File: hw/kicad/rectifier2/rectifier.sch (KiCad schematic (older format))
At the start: 10 parts, among them P1 CONN_01X03, P2 CONN_01X02, P3 CONN_01X02

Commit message: rectifier 2
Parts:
- C1, C2: footprint stmbl:C_Radial_D26_L45_P10 -> Capacitors_ThroughHole:CP_Radial_D35.0mm_P10.00mm_SnapIn
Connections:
- net Earth_Protective: now also P1.3 (P3); no longer P1.1 (P1)
- net at C1.1, C2.1, D1.3 (+): now also P3.2 (P2); no longer P3.1 (P1)
- net at C1.2, C2.2, D1.1 (-): now also P3.1 (P1); no longer P3.2 (P2)
- net at F1.2: now also P1.1 (P1); no longer P1.3 (P3)
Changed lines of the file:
@@
 LIBS:contrib
 LIBS:valves
-LIBS:stmbl
 LIBS:relays
 LIBS:rectifier-cache
-EELAYER 26 0
+EELAYER 25 0
 EELAYER END
 $Descr A4 11693 8268
@@
 F 3 "" H 6200 2150 50  0001 C CNN
 	1    8750 2700
-	1    0    0    -1
+	1    0    0    1
 $EndComp
 $Comp
@@
 F 3 "" H -1100 -2550 50  0001 C CNN
 	1    1850 2900
-	-1   0    0    1
+	-1   0    0    -1
 $EndComp
 $Comp
@@
 F 0 "C1" H 7868 2746 50  0000 L CNN
 F 1 "CP" H 7868 2655 50  0000 L CNN
-F 2 "stmbl:C_Radial_D26_L45_P10" H 5688 750 50  0001 C CNN
+F 2 "Capacitors_ThroughHole:CP_Radial_D35.0mm_P10.00mm_SnapIn" H 5688 750 50  0001 C CNN
 F 3 "" H 5650 900 50  0001 C CNN
 	1    7750 2700
@@
 F 0 "C2" H 8268 2746 50  0000 L CNN
 F 1 "CP" H 8268 2655 50  0000 L CNN
-F 2 "stmbl:C_Radial_D26_L45_P10" H 5488 850 50  0001 C CNN
+F 2 "Capacitors_ThroughHole:CP_Radial_D35.0mm_P10.00mm_SnapIn" H 5488 850 50  0001 C CNN
 F 3 "" H 5450 1000 50  0001 C CNN
 	1    8150 2700

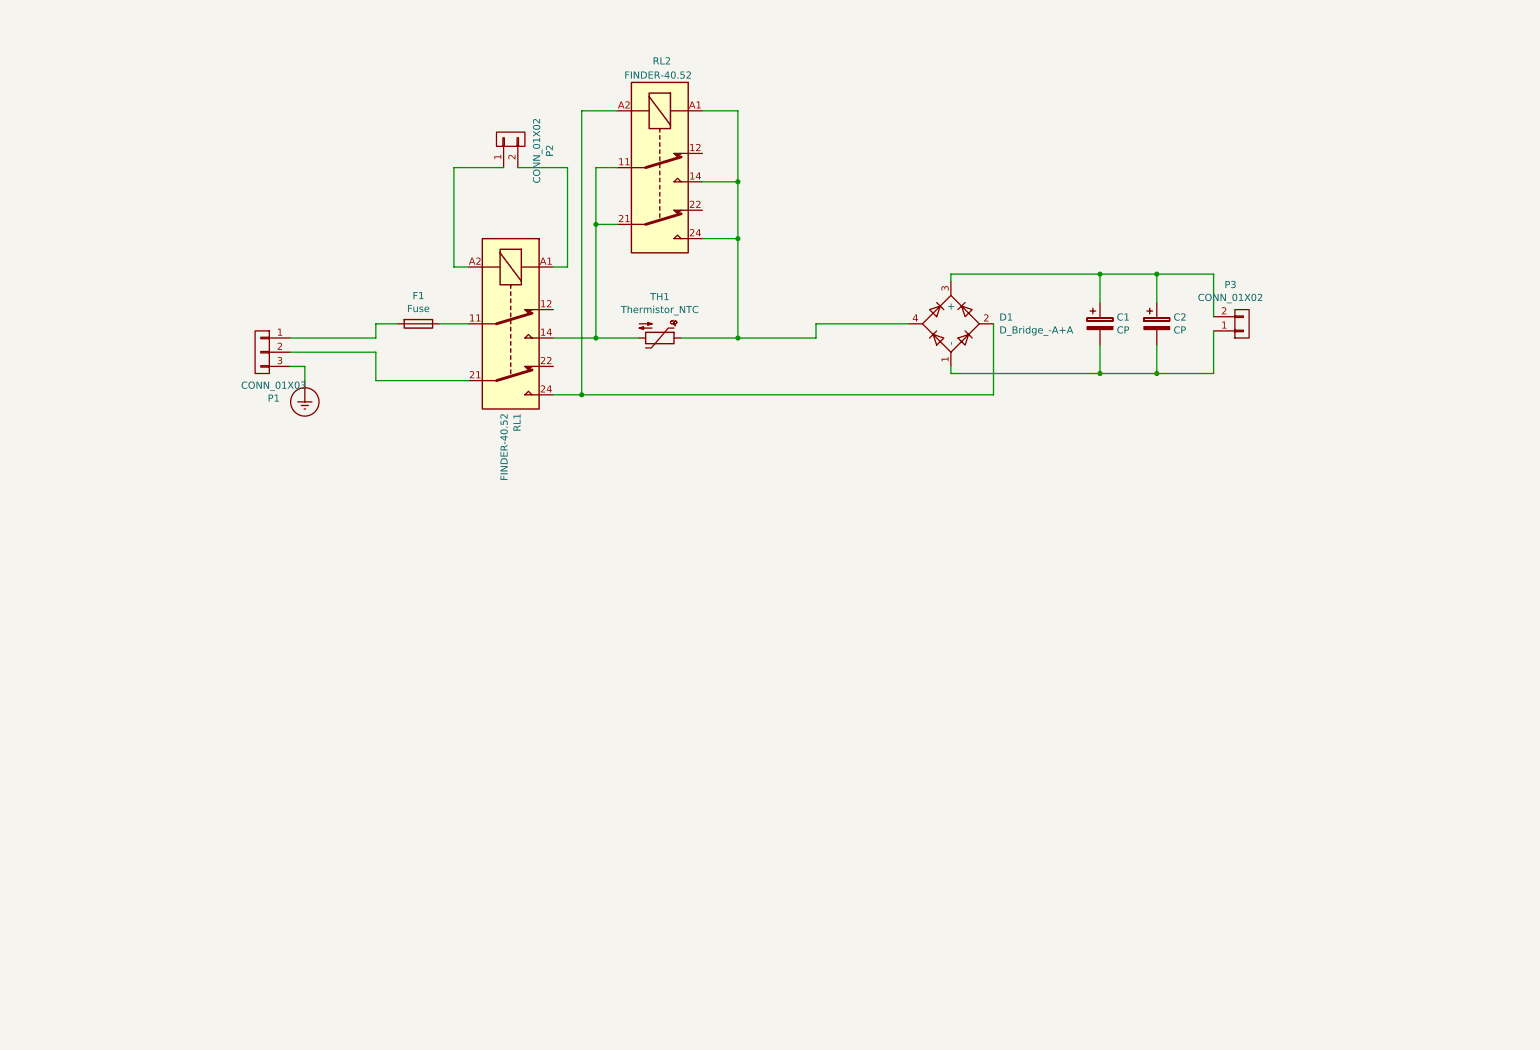
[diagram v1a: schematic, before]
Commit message: Added STM32F042 to rectifier for brake support and proper inrush protection.
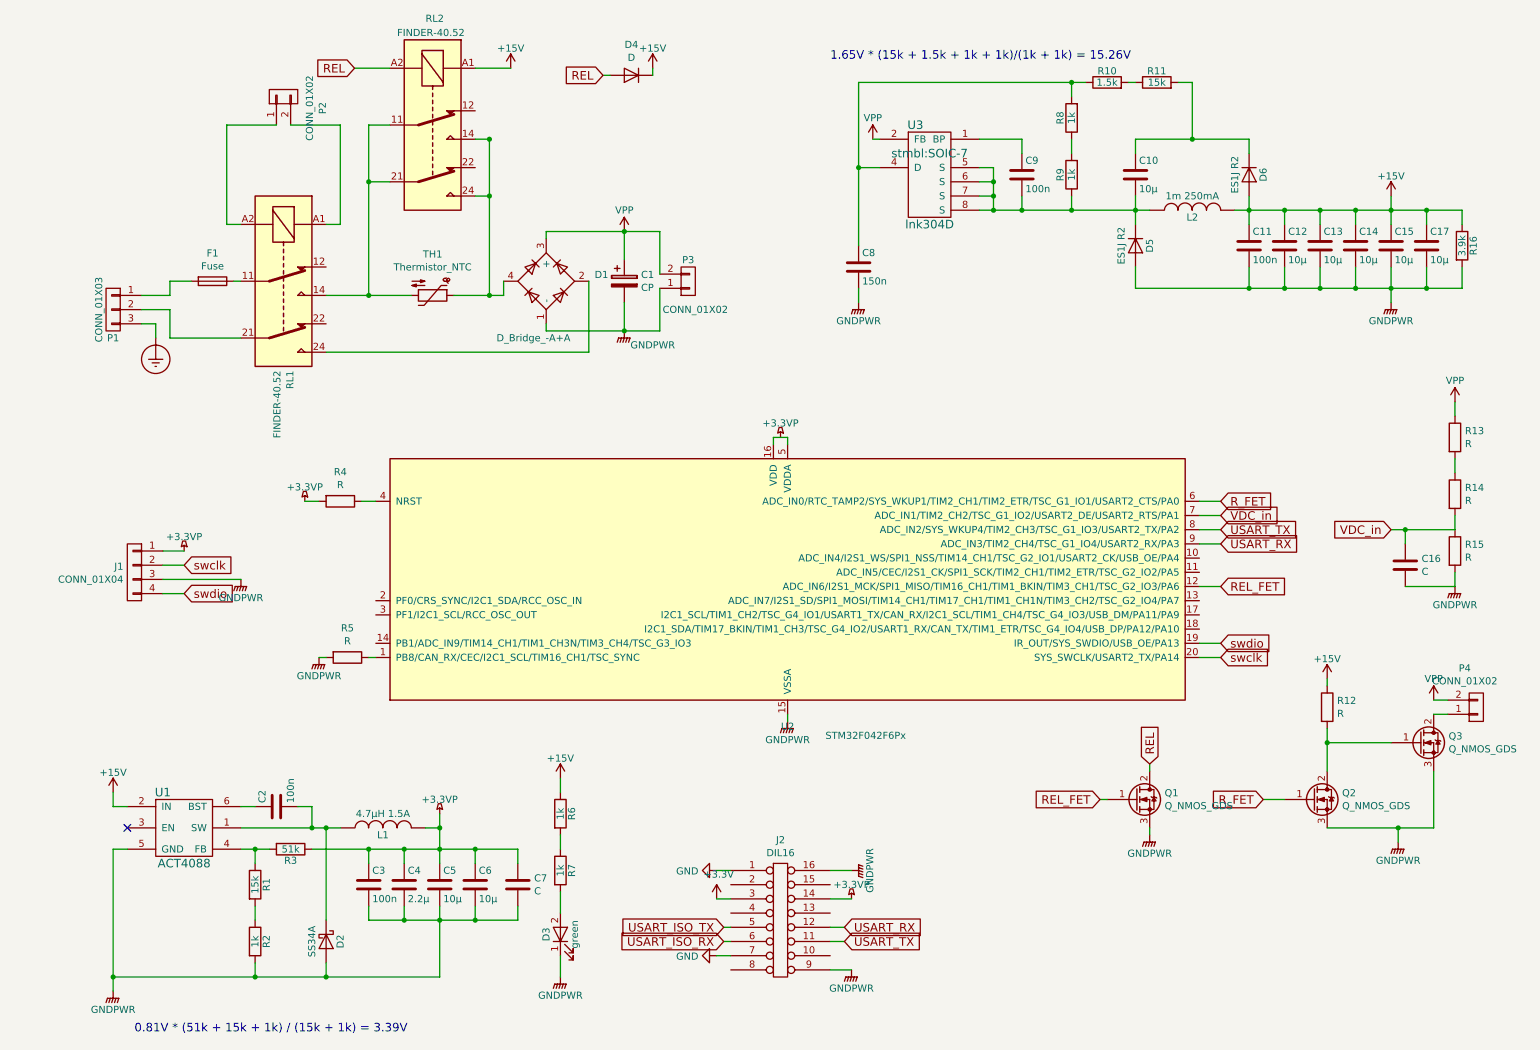
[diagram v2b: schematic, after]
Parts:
- removed C2: CP, Capacitors_ThroughHole:CP_Radial_D35.0mm_P10.00mm_SnapIn, symbol CP
- added C10, C12, C13, C14, C15, C17, C5, C6: 10µ, stmbl:C_0805, symbol C
- added C11, C2, C3, C9: 100n, stmbl:C_0603, symbol C
- added C16, C7: C, symbol C
- added C4: 2.2µ, stmbl:C_0603, symbol C
- added C8: 150n, stmbl:C_1808, symbol C
- added D2: SS34A, stmbl:SMA_Standard, symbol D_Schottky
- added D3: green, stmbl:LED-0805-SIDE, symbol LED
- added D4: D, symbol D
- added D5, D6: ES1J R2, stmbl:SMA_Standard, symbol D
- added J1: CONN_01X04, symbol CONN_01X04
- added J2: DIL16, symbol DIL16
- added L1: 4.7µH 1.5A, stmbl:SMD_INDUCTOR_32x25, symbol INDUCTOR
- added L2: 1m 250mA, stmbl:NPI31W, symbol INDUCTOR
- added P4: CONN_01X02, stmbl:RM5.08_1x2, symbol CONN_01X02
- added Q1, Q2, Q3: Q_NMOS_GDS, symbol Q_NMOS_GDS
- added R1, R11: 15k, stmbl:R_0603, symbol R
- added R10: 1.5k, stmbl:R_0603, symbol R
- added R12, R13, R14, R15, R4, R5: R, symbol R
- added R16: 3.9k, stmbl:R_0603, symbol R
- added R2, R6, R7, R8, R9: 1k, stmbl:R_0603, symbol R
- added R3: 51k, stmbl:R_0603, symbol R
- added U1: ACT4088, TO_SOT_Packages_SMD:SOT-23-6, symbol ACT4088
- added U2: STM32F042F6Px, Housings_SSOP:TSSOP-20_4.4x6.5mm_Pitch0.65mm, symbol STM32F042F6Px
- added U3: lnk304D, stmbl:SOIC-7, symbol lnk304D
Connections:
- net GNDPWR: now reaches C1.2, D1.1 (-), P3.1 (P1)
- net GNDPWR: now also C11.2, C12.2, C13.2, C14.2, C15.2, C16.2, C17.2, C3.2, C4.2, C5.2, C6.2, C7.2, C8.2, D2.2 (A), D3.1 (K), D5.2 (A), J1.3 (P3), J2.16, J2.9, Q1.3 (S), Q2.3 (S), Q3.3 (S), R15.2, R16.2, R2.2, R5.2, U1.5 (GND), U2.15 (VSSA)
- net VPP: now reaches C1.1, D1.3 (+), P3.2 (P2)
- net VPP: now also P4.2 (P2), R13.1, U3.2 (FB)
- net at D1.2, RL1.24: no longer RL2.A2
- net at D1.4, RL2.14, RL2.24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: no longer RL2.A1
- new net: C10.2, C9.2, D5.1 (K), L2.1, R9.1, U3.5 (S), U3.6 (S), U3.7 (S), U3.8 (S)
- new net: C10.1, D6.1 (K), R11.2
- new net: C9.1, U3.1 (BP)
- new net: R8.1, R9.2
- new net: R10.2, R11.1
- new net: D3.2 (A), R7.2
- new net: R6.2, R7.1
- new net: R1.1, R3.2, U1.4 (FB)
- new net: R1.2, R2.1
- new net: C2.2, D2.1 (K), L1.1, U1.1 (SW)
- new net: C2.1, U1.6 (BST)
- new net: C8.1, R10.1, R8.2, U3.4 (D)
- new net: R5.1, U2.1 (PB8/CAN_RX/CEC/I2C1_SCL/TIM16_CH1/TSC_SYNC)
- new net: U2.16 (VDD), U2.5 (VDDA)
- new net: R4.1, U2.4 (NRST)
- new net: R13.2, R14.1
- new net: Q2.2 (D), Q3.1 (G), R12.2
- new net: P4.1 (P1), Q3.2 (D)
- new net +15V: C11.1, C12.1, C13.1, C14.1, C15.1, C17.1, D4.1 (K), D6.2 (A), L2.2, R12.1, R16.1, R6.1, RL2.A1, U1.2 (IN)
- new net +3.3VP: C3.1, C4.1, C5.1, C6.1, C7.1, J1.1 (P1), J2.14, L1.2, R3.1, R4.2
- new net +3V3: J2.3
- new net GND: J2.1, J2.7
- new net REL: D4.2 (A), Q1.2 (D), RL2.A2
- new net REL_FET: Q1.1 (G), U2.12 (ADC_IN6/I2S1_MCK/SPI1_MISO/TIM16_CH1/TIM1_BKIN/TIM3_CH1/TSC_G2_IO3/PA6)
- new net R_FET: Q2.1 (G), U2.6 (ADC_IN0/RTC_TAMP2/SYS_WKUP1/TIM2_CH1/TIM2_ETR/TSC_G1_IO1/USART2_CTS/PA0)
- new net USART_ISO_RX: J2.6
- new net USART_ISO_TX: J2.5
- new net USART_RX: J2.12, U2.9 (ADC_IN3/TIM2_CH4/TSC_G1_IO4/USART2_RX/PA3)
- new net USART_TX: J2.11, U2.8 (ADC_IN2/SYS_WKUP4/TIM2_CH3/TSC_G1_IO3/USART2_TX/PA2)
- new net VDC_in: C16.1, R14.2, R15.1, U2.7 (ADC_IN1/TIM2_CH2/TSC_G1_IO2/USART2_DE/USART2_RTS/PA1)
- new net swclk: J1.2 (P2), U2.20 (SYS_SWCLK/USART2_TX/PA14)
- new net swdio: J1.4 (P4), U2.19 (IR_OUT/SYS_SWDIO/USB_OE/PA13)
- no-connect marks 0 -> 1
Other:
- note added: "0.81V * (51k + 15k + 1k) / (15k + 1k) = 3.39V"
- note added: "1.65V * (15k + 1.5k + 1k + 1k)/(1k + 1k) = 15.26V"
- moved on the sheet: C1, D1, F1, P1, P2, P3, RL1, RL2, TH1

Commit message: Change relay drive to 24V and add enable feedback
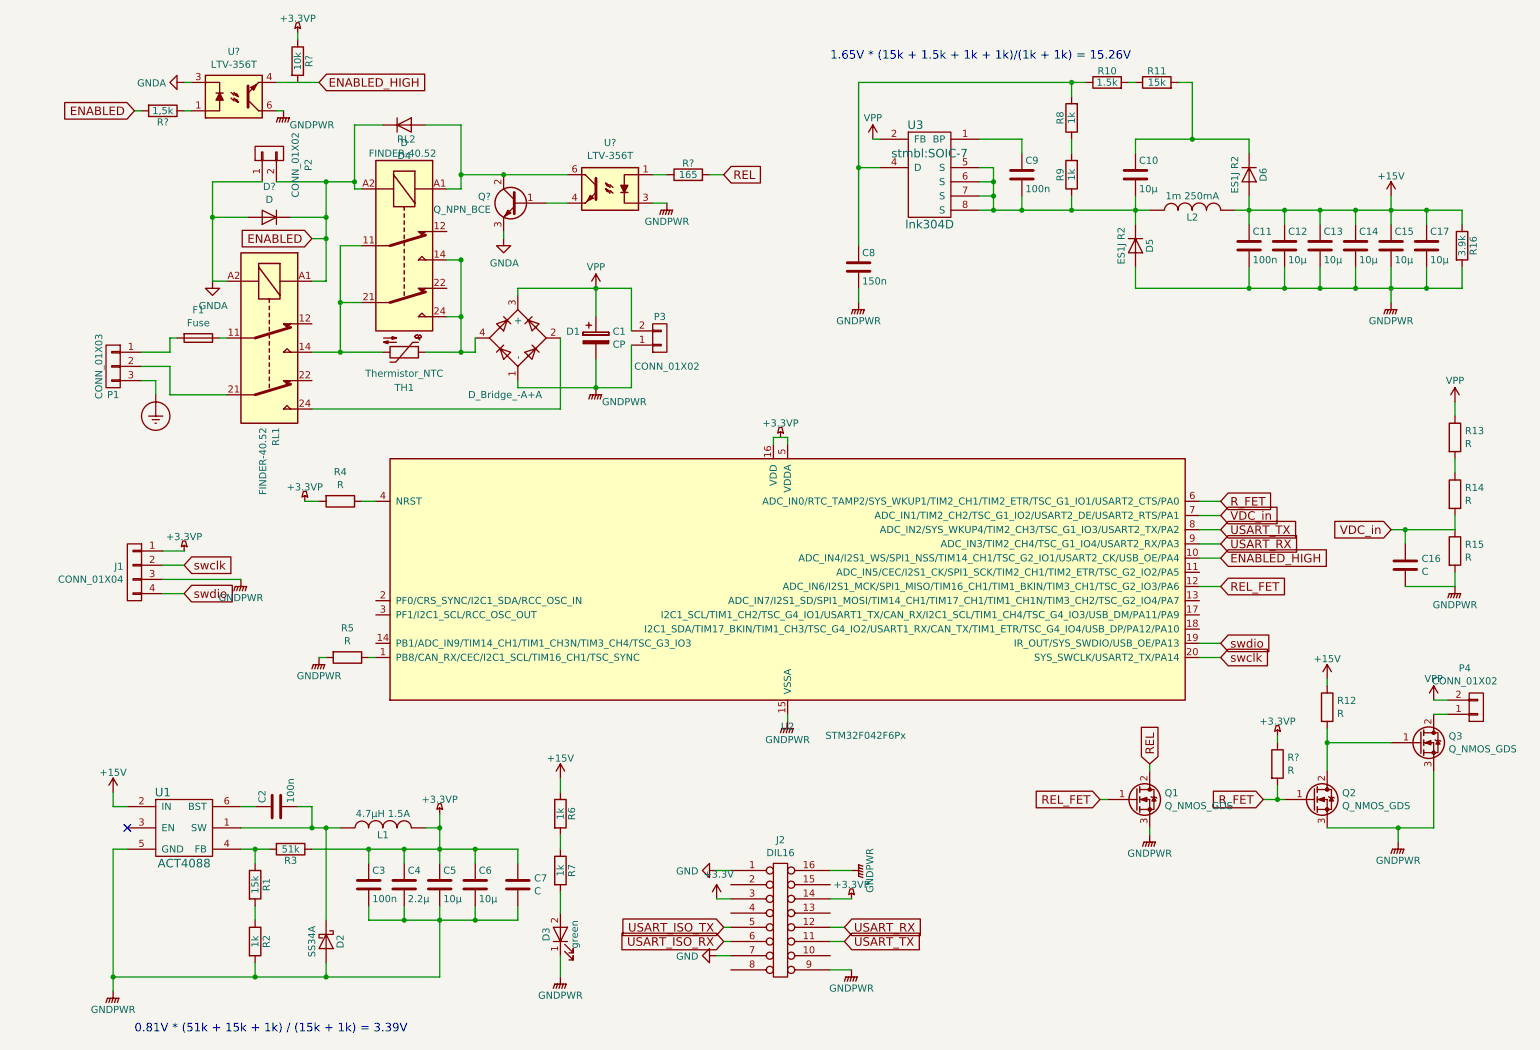
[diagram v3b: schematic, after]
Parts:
- added D?: D, symbol D
- added Q?: Q_NPN_BCE, symbol Q_NPN_BCE
- added R?: R, symbol R
- added R?: 165, stmbl:R_0603, symbol R
- added R?: 10k, stmbl:R_0603, symbol R
- added R?: 1,5k, stmbl:R_0603, symbol R
- added U? (x2): LTV-356T, Housings_DIP:DIP-6_W7.62mm_SMD, symbol LTV-356T
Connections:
- net +15V: no longer D4.1 (K), RL2.A1
- net +3.3VP: now also R?.1, R?.1
- net GNDPWR: now also U?.3, U?.6
- net REL: now also R?.2; no longer D4.2 (A), RL2.A2
- net R_FET: now also R?.2
- net GNDA: now reaches P2.1 (P1), RL1.A2
- net GNDA: now also D?.2 (A), Q?.3 (E), U?.3
- net ENABLED: now reaches P2.2 (P2), RL1.A1
- net ENABLED: now also D4.1 (K), RL2.A2, D?.1 (K), R?.2
- net ENABLED_HIGH: now reaches U2.10 (ADC_IN4/I2S1_WS/SPI1_NSS/TIM14_CH1/TSC_G2_IO1/USART2_CK/USB_OE/PA4)
- net ENABLED_HIGH: now also U?.4
- new net: D4.2 (A), Q?.2 (C), RL2.A1, U?.6
- new net: R?.1, U?.1 (x2)
- new net: Q?.1 (B), U?.4
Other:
- moved on the sheet: C1, D1, D4, F1, P1, P2, P3, RL1, RL2, TH1

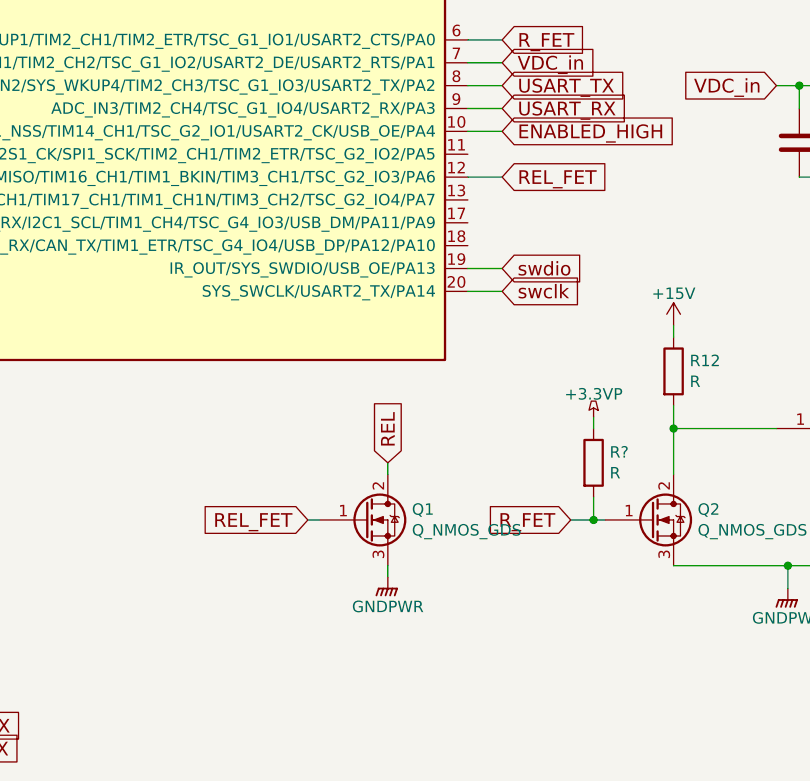
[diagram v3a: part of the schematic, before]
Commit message: Small mistake in schematic
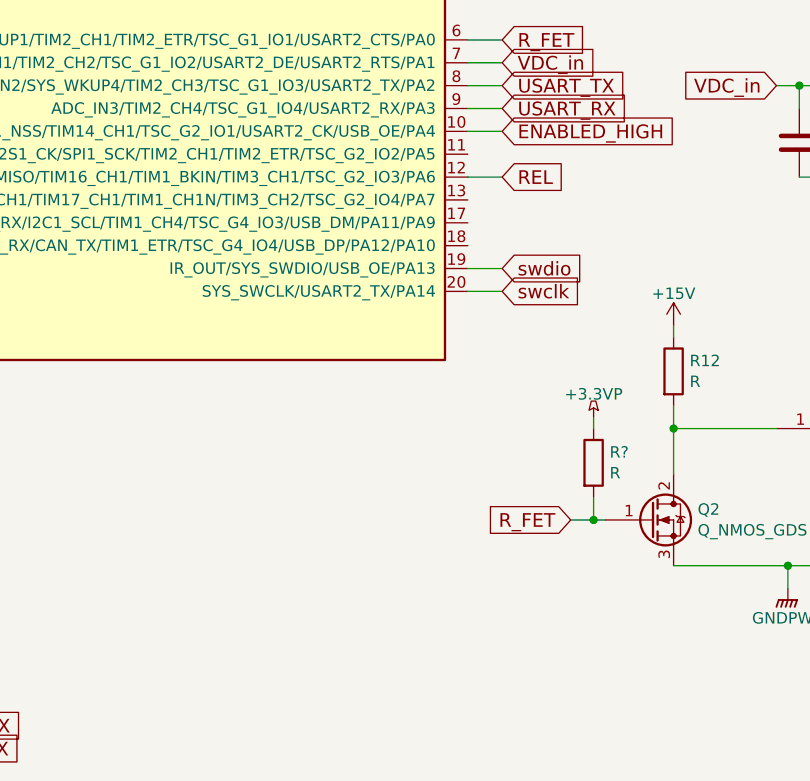
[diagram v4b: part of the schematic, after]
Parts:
- removed Q1: Q_NMOS_GDS, symbol Q_NMOS_GDS
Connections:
- net REL_FET is gone; now on net REL: U2.12 (ADC_IN6/I2S1_MCK/SPI1_MISO/TIM16_CH1/TIM1_BKIN/TIM3_CH1/TSC_G2_IO3/PA6)
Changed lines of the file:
@@
 	8900 6050 9050 6050
-$Comp
-L Q_NMOS_GDS Q1
-U 1 1 595A3313
-P 8000 6050
-F 0 "Q1" H 8205 6096 50  0000 L CNN
-F 1 "Q_NMOS_GDS" H 8205 6005 50  0000 L CNN
-F 2 "" H 8200 6150 50  0001 C CNN
-F 3 "" H 8000 6050 50  0001 C CNN
-	1    8000 6050
-	1    0    0    -1
-$EndComp
-Text GLabel 8100 5800 1    60   Input ~ 0
-REL
-$Comp
-L GNDPWR #PWR25
-U 1 1 595A3BC7
-P 8100 6300
-F 0 "#PWR25" H 8100 6100 50  0001 C CNN
-F 1 "GNDPWR" H 8100 6170 50  0000 C CNN
-F 2 "" H 8100 6250 60  0000 C CNN
-F 3 "" H 8100 6250 60  0000 C CNN
-	1    8100 6300
-	1    0    0    -1
-$EndComp
 $Comp
 L D D4
@@
 Text GLabel 5100 1650 2    60   Input ~ 0
 REL
-Wire Wire Line
-	8100 6300 8100 6250
-Wire Wire Line
-	8100 5850 8100 5800
-Text GLabel 7750 6050 0    60   Input ~ 0
-REL_FET
-Wire Wire Line
-	7750 6050 7800 6050
 $Comp
 L R R4
@@
 Wire Wire Line
 	8450 4050 8600 4050
-Text GLabel 8600 4550 2    60   Input ~ 0
-REL_FET
 Text GLabel 8600 3950 2    60   Input ~ 0
 R_FET
 Wire Wire Line
 	8450 3950 8600 3950
-Wire Wire Line
-	8450 4550 8600 4550
 Text GLabel 8600 4950 2    60   Input ~ 0
 swdio
@@
 Wire Wire Line
 	8450 4350 8600 4350
+Wire Wire Line
+	8450 4550 8600 4550
+Text GLabel 8600 4550 2    60   Input ~ 0
+REL
 $EndSCHEMATC
